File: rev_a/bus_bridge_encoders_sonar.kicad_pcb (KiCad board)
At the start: 2 copper layers, 50 x 50 mm, 33 parts, among them J1 POWER_SELECT, U1 LM2940, U2 LTV-826, U3 LTV-826, U4 LTV-826, U5 754410

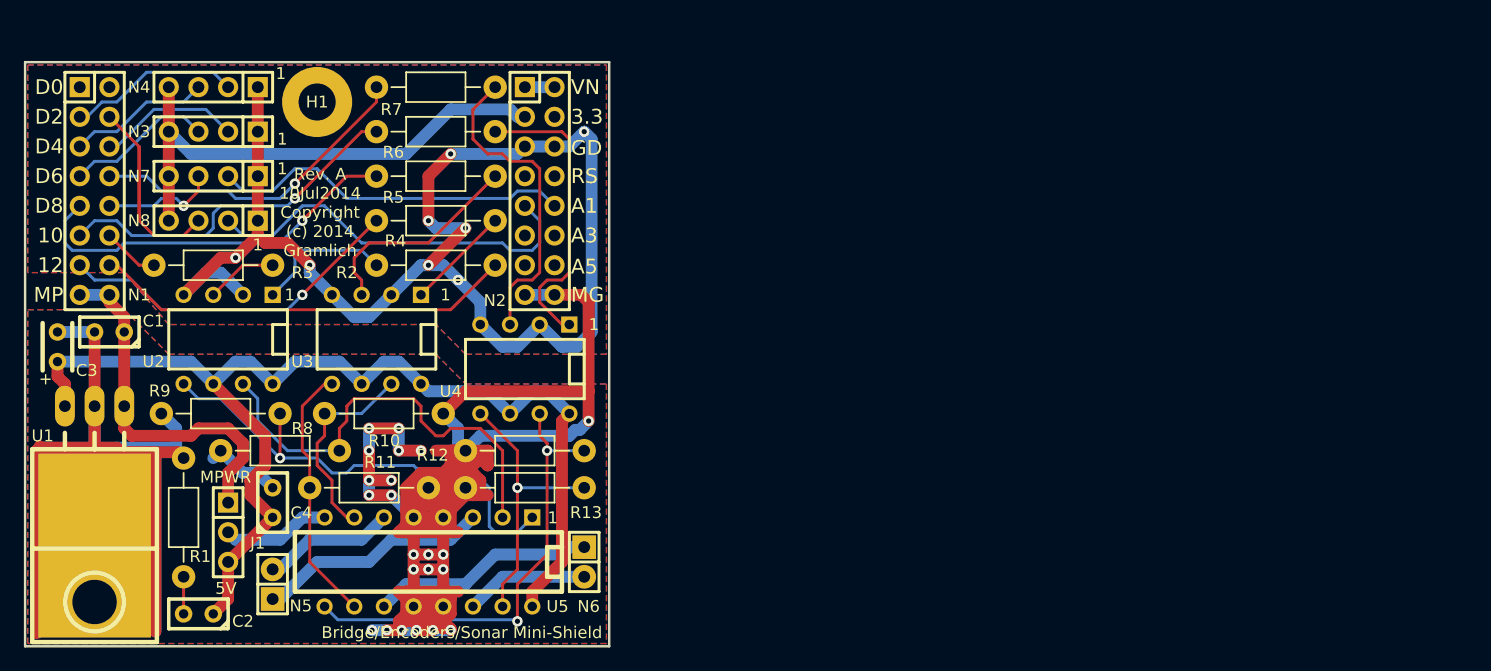
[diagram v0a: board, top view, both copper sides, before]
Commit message: Finished Rev. A board layout.
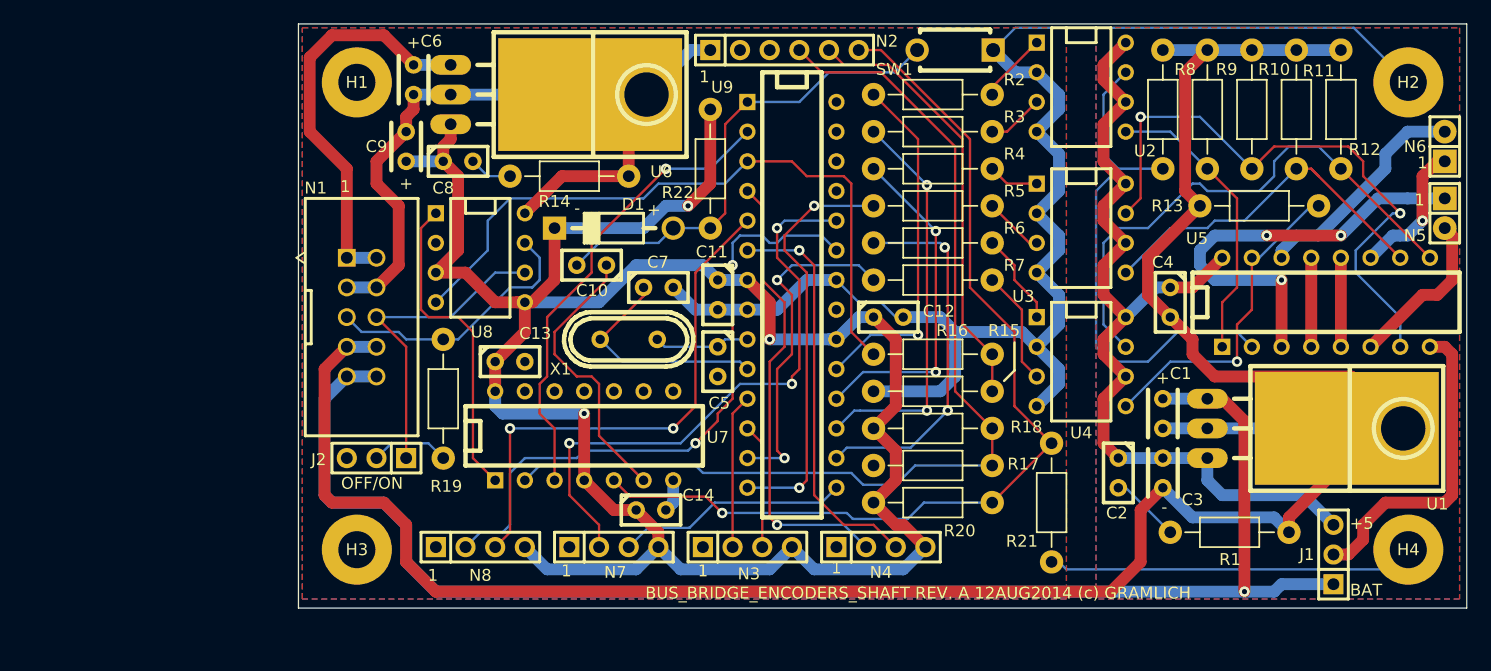
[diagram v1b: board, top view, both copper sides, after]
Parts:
- added C10: .1uF, Bus_Bridge_Encoders_Sonar_Rev_A:Capacitor3MMDiscRM2.5, F.Cu at (125.1, 120.7)
- added C11: .1uF, Bus_Bridge_Encoders_Sonar_Rev_A:Capacitor3MMDiscRM2.5, F.Cu at (135.9, 123.2)
- added C12: .1uF, Bus_Bridge_Encoders_Sonar_Rev_A:Capacitor3MMDiscRM2.5, F.Cu at (150.5, 125.1)
- added C13: .1uF, Bus_Bridge_Encoders_Sonar_Rev_A:Capacitor3MMDiscRM2.5, F.Cu at (118.1, 128.9)
- added C14: .1uF, Bus_Bridge_Encoders_Sonar_Rev_A:Capacitor3MMDiscRM2.5, F.Cu at (130.2, 141.6)
- added C5: 18pF, Bus_Bridge_Encoders_Sonar_Rev_A:Capacitor3MMDiscRM2.5, F.Cu at (135.9, 128.9)
- added C6: 22uF, Bus_Bridge_Encoders_Sonar_Rev_A:Capacitor4x3RM2-5_RevB, F.Cu at (109.9, 104.8)
- added C7: 18pF, Bus_Bridge_Encoders_Sonar_Rev_A:Capacitor3MMDiscRM2.5, F.Cu at (130.8, 122.6)
- added C8: .1uF, Bus_Bridge_Encoders_Sonar_Rev_A:Capacitor3MMDiscRM2.5, F.Cu at (113.7, 111.8)
- added C9: 22uF, Bus_Bridge_Encoders_Sonar_Rev_A:Capacitor4x3RM2-5_RevB, F.Cu at (109.2, 110.5)
- added D1: SD101C-TR, Bus_Bridge_Encoders_Sonar_Rev_A:Diode_DO-41_SOD81_Horizontal_RM10, F.Cu at (127.0, 117.5)
- added H2: 3MM_HOLE, Bus_Bridge_Encoders_Sonar_Rev_A:MountingHole_3mm, F.Cu at (195.0, 105.0)
- added H3: 3MM_HOLE, Bus_Bridge_Encoders_Sonar_Rev_A:MountingHole_3mm, F.Cu at (105.0, 145.0)
- added H4: 3MM_HOLE, Bus_Bridge_Encoders_Sonar_Rev_A:MountingHole_3mm, F.Cu at (195.0, 145.0)
- added J2: TERMINATE_JUMPER, Bus_Bridge_Encoders_Sonar_Rev_A:Pin_Header_Straight_1x03, F.Cu at (106.7, 137.2)
- added R14: .47, Bus_Bridge_Encoders_Sonar_Rev_A:Resistor_Horizontal_400, F.Cu at (123.2, 113.0)
- added R15: 22K, Bus_Bridge_Encoders_Sonar_Rev_A:Resistor_Horizontal_400, F.Cu at (154.3, 128.3)
- added R16: 33K, Bus_Bridge_Encoders_Sonar_Rev_A:Resistor_Horizontal_400, F.Cu at (154.3, 131.4)
- added R17: 22K, Bus_Bridge_Encoders_Sonar_Rev_A:Resistor_Horizontal_400, F.Cu at (154.3, 134.6)
- added R18: 33K, Bus_Bridge_Encoders_Sonar_Rev_A:Resistor_Horizontal_400, F.Cu at (154.3, 137.8)
- added R19: .47, Bus_Bridge_Encoders_Sonar_Rev_A:Resistor_Horizontal_400, F.Cu at (112.4, 132.1)
- added R20: 22K, Bus_Bridge_Encoders_Sonar_Rev_A:Resistor_Horizontal_400, F.Cu at (154.3, 141.0)
- added R21: 33K, Bus_Bridge_Encoders_Sonar_Rev_A:Resistor_Horizontal_400, F.Cu at (164.5, 141.0)
- added R22: 10K, Bus_Bridge_Encoders_Sonar_Rev_A:Resistor_Horizontal_400, F.Cu at (135.3, 112.4)
- added SW1: MJTP1243, Bus_Bridge_Encoders_Sonar_Rev_A:Button_6.5MM, F.Cu at (156.2, 102.2)
- added U6: LM2940, Bus_Bridge_Encoders_Sonar_Rev_A:TO-220_Neutral123_Horizontal_LargePads, F.Cu at (113.0, 106.0)
- added U7: 74HCT08, Bus_Bridge_Encoders_Sonar_Rev_A:DIP-14__300, F.Cu at (124.5, 135.3)
- added U8: MCP2562, Bus_Bridge_Encoders_Sonar_Rev_A:DIP-8__300, F.Cu at (115.6, 120.0)
- added U9: ATMEGA328_DIP28, Bus_Bridge_Encoders_Sonar_Rev_A:DIP-28__300, F.Cu at (142.2, 123.2)
- added X1: CRYSTAL, Bus_Bridge_Encoders_Sonar_Rev_A:Crystal_HC49-U_Vertical, F.Cu at (128.3, 127.0)
- C1: footprint Mini_Bridge_Encoders_Sonar_Rev_B:Capacitor3MMDiscRM2.5 -> Bus_Bridge_Encoders_Sonar_Rev_A:Capacitor4x3RM2-5_RevB
- C2, C4: footprint Mini_Bridge_Encoders_Sonar_Rev_B:Capacitor3MMDiscRM2.5 -> Bus_Bridge_Encoders_Sonar_Rev_A:Capacitor3MMDiscRM2.5
- C3: footprint Mini_Bridge_Encoders_Sonar_Rev_B:Capacitor4x3RM2-5_RevB -> Bus_Bridge_Encoders_Sonar_Rev_A:Capacitor4x3RM2-5_RevB
- G1: footprint Mini_Bridge_Encoders_Sonar_Rev_B:OSHW_LOGO_400mil -> Bus_Bridge_Encoders_Sonar_Rev_A:OSHW_LOGO_400mil
- H1: footprint Mini_Bridge_Encoders_Sonar_Rev_B:MountingHole_3mm -> Bus_Bridge_Encoders_Sonar_Rev_A:MountingHole_3mm
- J1: footprint Mini_Bridge_Encoders_Sonar_Rev_B:Pin_Header_Straight_1x03 -> Bus_Bridge_Encoders_Sonar_Rev_A:Pin_Header_Straight_1x03
- N1: value MS_DATA_HEADER -> BUS_SLAVE_HEADER; footprint Mini_Bridge_Encoders_Sonar_Rev_B:Pin_Header_Straight_2x08 -> Bus_Bridge_Encoders_Sonar_Rev_A:Pin_Header_Straight_2x05_Shrouded
- N2: value MS_PWR_HEADER -> FTDI_HEADER; footprint Mini_Bridge_Encoders_Sonar_Rev_B:Pin_Header_Straight_2x08 -> Bus_Bridge_Encoders_Sonar_Rev_A:Pin_Header_Straight_1x06
- N3, N4, N7, N8: footprint Mini_Bridge_Encoders_Sonar_Rev_B:Pin_Header_Straight_1x04 -> Bus_Bridge_Encoders_Sonar_Rev_A:Pin_Header_Straight_1x04
- N5, N6: footprint Mini_Bridge_Encoders_Sonar_Rev_B:Pin_Header_Straight_1x02 -> Bus_Bridge_Encoders_Sonar_Rev_A:Pin_Header_Straight_1x02
- R1, R10, R11, R12, R13, R2, R3, R4, R5, R6, R7, R8, R9: footprint Mini_Bridge_Encoders_Sonar_Rev_B:Resistor_Horizontal_400 -> Bus_Bridge_Encoders_Sonar_Rev_A:Resistor_Horizontal_400
- U1: footprint Mini_Bridge_Encoders_Sonar_Rev_B:TO-220_Neutral123_Horizontal_LargePads -> Bus_Bridge_Encoders_Sonar_Rev_A:TO-220_Neutral123_Horizontal_LargePads
- U2, U3, U4: footprint Mini_Bridge_Encoders_Sonar_Rev_B:DIP-8__300 -> Bus_Bridge_Encoders_Sonar_Rev_A:DIP-8__300
- U5: footprint Mini_Bridge_Encoders_Sonar_Rev_B:DIP-16__300 -> Bus_Bridge_Encoders_Sonar_Rev_A:DIP-16__300
- moved N5 105.2 mm to (198.1, 116.2), turned to 270 degrees
- moved G1 102.2 mm to (184.8, 134.0)
- moved U1 95.3 mm to (177.8, 134.6), turned to 270 degrees
- moved C3 95.2 mm to (174.0, 138.4), turned to 270 degrees
- moved J1 94.6 mm to (188.6, 145.4), turned to 90 degrees
- moved C1 90.4 mm to (174.0, 133.3), turned to 270 degrees
- moved R1 89.5 mm to (179.7, 143.5), turned to 180 degrees
- moved R9 88.4 mm to (177.8, 107.3), turned to 270 degrees
- moved R11 85.7 mm to (185.4, 107.3), turned to 270 degrees
- moved N6 81.8 mm to (198.1, 110.5), turned to 90 degrees
- moved R8 81.0 mm to (174.0, 107.3), turned to 270 degrees
- moved U5 80.0 mm to (188.0, 123.8), turned to 0 degrees
- moved C2 79.7 mm to (170.2, 138.4), turned to 270 degrees
- moved R10 78.7 mm to (181.6, 107.3), turned to 270 degrees
- moved C4 78.7 mm to (174.6, 123.8), turned to 270 degrees
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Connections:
- C1 pad 1: /MPWR -> /BPWR
- C1 pad 2: /MGND -> /BGND
- C3 pad 2: /MGND -> /BGND
- C4 pad 2: /MGND -> /BGND
- J1 pad 1: /MPWR -> /BPWR
- N1 pad 1: (no net) -> /LPWR
- N1 pad 10: /D9 -> /BPWR
- N1 pad 2: (no net) -> /LPWR
- N1 pad 3: /D2 -> GND
- N1 pad 4: /D3 -> GND
- N1 pad 5: /D4 -> Net-(N1-Pad5)
- N1 pad 6: /D5 -> Net-(J2-Pad1)
- N1 pad 7: /D6 -> /BGND
- N1 pad 8: /D7 -> /BGND
- N1 pad 9: /D8 -> /BPWR
- N2 pad 1: /VIN -> GND
- N2 pad 2: /VIN -> Net-(N2-Pad2)
- N2 pad 3: /5V -> Net-(N2-Pad3)
- N2 pad 4: (no net) -> Net-(N2-Pad4)
- N2 pad 5: GND -> Net-(N2-Pad5)
- N2 pad 6: GND -> Net-(N2-Pad6)
- N3 pad 4: /5V -> +5V
- N4 pad 4: /5V -> +5V
- N7 pad 4: /5V -> +5V
- N8 pad 4: /5V -> +5V
- R1 pad 1: /MGND -> /BGND
- R10 pad 1: /MGND -> /BGND
- R11 pad 1: /MGND -> /BGND
- R12 pad 1: /MGND -> /BGND
- R13 pad 1: /MGND -> /BGND
- R8 pad 1: /MGND -> /BGND
- R9 pad 1: /MGND -> /BGND
- U1 pad 1: /MPWR -> /BPWR
- U1 pad 2: /MGND -> /BGND
- U5 pad 12: /MGND -> /BGND
- U5 pad 13: /MGND -> /BGND
- U5 pad 4: /MGND -> /BGND
- U5 pad 5: /MGND -> /BGND
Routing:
- net /MGND: track 374.4 -> 0.00 mm, vias 22 -> 0
- net /BGND: track 0.00 -> 228.4 mm
- net +5V: track 0.00 -> 190.0 mm, vias 0 -> 3
- net /BPWR: track 0.00 -> 127.8 mm, vias 0 -> 1
- net GND: track 111.7 -> 226.9 mm, vias 8 -> 0
- net Net-(N2-Pad4): track 0.00 -> 87.3 mm
- net Net-(N2-Pad6): track 0.00 -> 83.1 mm, vias 0 -> 1
- net /TXD: track 0.00 -> 58.2 mm
- net /5V: track 44.5 -> 0.00 mm
- net /~RESET: track 0.00 -> 41.2 mm
- net /RXD: track 0.00 -> 40.0 mm, vias 0 -> 1
- net Net-(N2-Pad5): track 0.00 -> 37.2 mm
- net /LPWR: track 0.00 -> 34.9 mm
- net Net-(R10-Pad2): track 17.6 -> 51.7 mm, vias 0 -> 2
- net /MPWR: track 31.3 -> 0.00 mm
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- added copper zone on B.Cu, net /BGND
- added copper zone on F.Cu, net /BGND
- removed copper zone on B.Cu, net /MGND
- removed copper zone on F.Cu, net /MGND
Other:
- board size 50 x 50 mm -> 100 x 50 mm
- net class Default: clearance 0.254 -> 0.2032; trace_width 0.254 -> 0.2032
- rule trace_clearance: 0.254 -> 0.2032
- rule trace_min: 0.254 -> 0.2032
- board text added: "+5"
- board text added: "-"
- board text added: "BAT"
- board text added: "BUS_BRIDGE_ENCODERS_SHAFT REV. A 12AUG2014 (c) GRAMLICH"
- board text added: "OFF/ON"
- board text removed: "10"
- board text removed: "12"
- board text removed: "3.3"
- board text removed: "5V"
- board text removed: "A1"
- board text removed: "A3"
- board text removed: "A5"
- board text removed: "Bridge/Encoders/Sonar Mini-Shield"
- board text removed: "D0"
- board text removed: "D2"
- board text removed: "D4"
- board text removed: "D6"
- board text removed: "D8"
- board text removed: "GD"
- board text removed: "MG"
- board text removed: "MP"
- board text removed: "MPWR"
- board text removed: "RS"
- board text removed: "Rev. A 10Jul2014 Copyright (c) 2014 Gramlich"
- board text removed: "VN"
